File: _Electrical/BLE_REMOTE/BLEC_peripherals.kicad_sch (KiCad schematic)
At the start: 15 parts, among them J5 Conn_01x02_Pin, J9 Display, Q3 NPN, Q4 BSS806NEH6327XTSA1

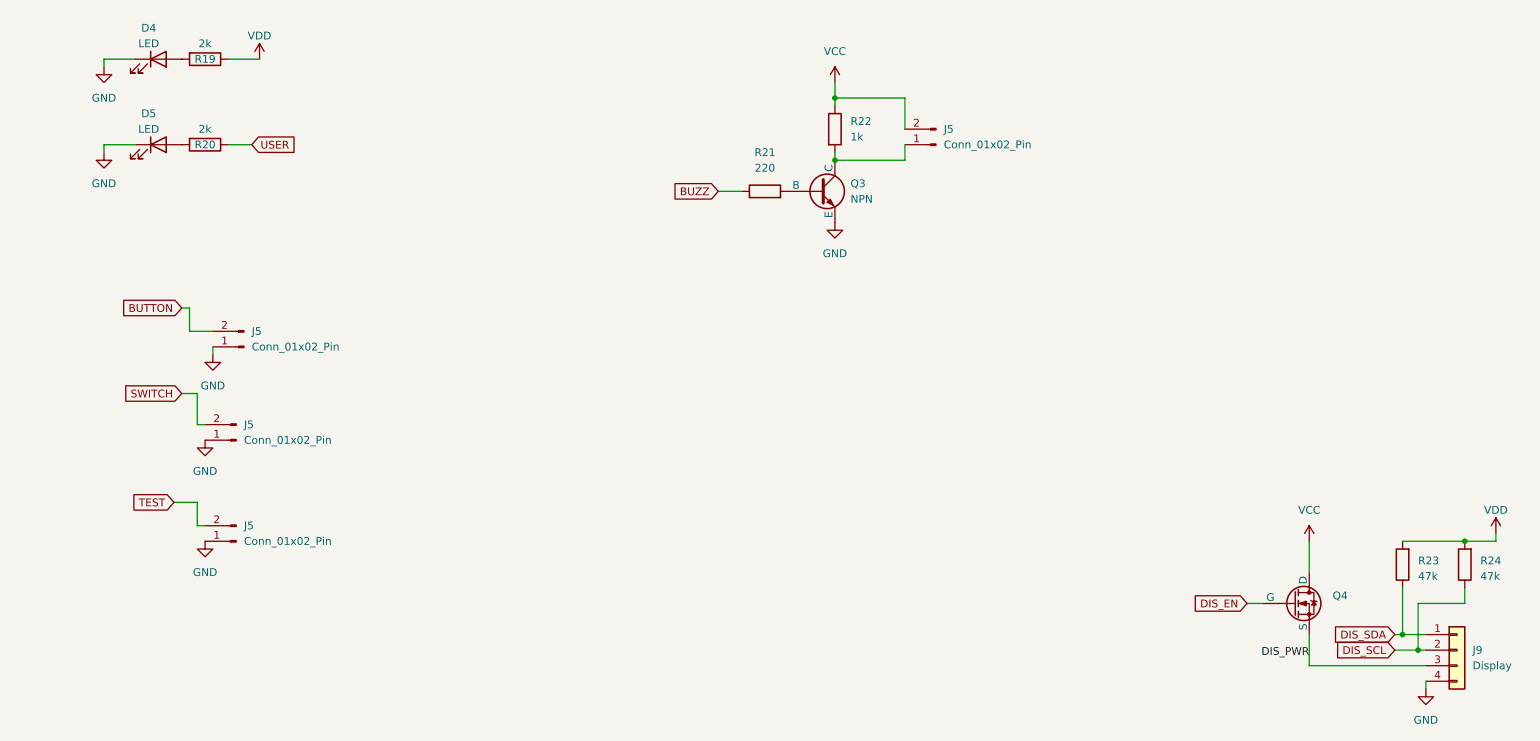
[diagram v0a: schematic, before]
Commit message: Added simulation and updated power button
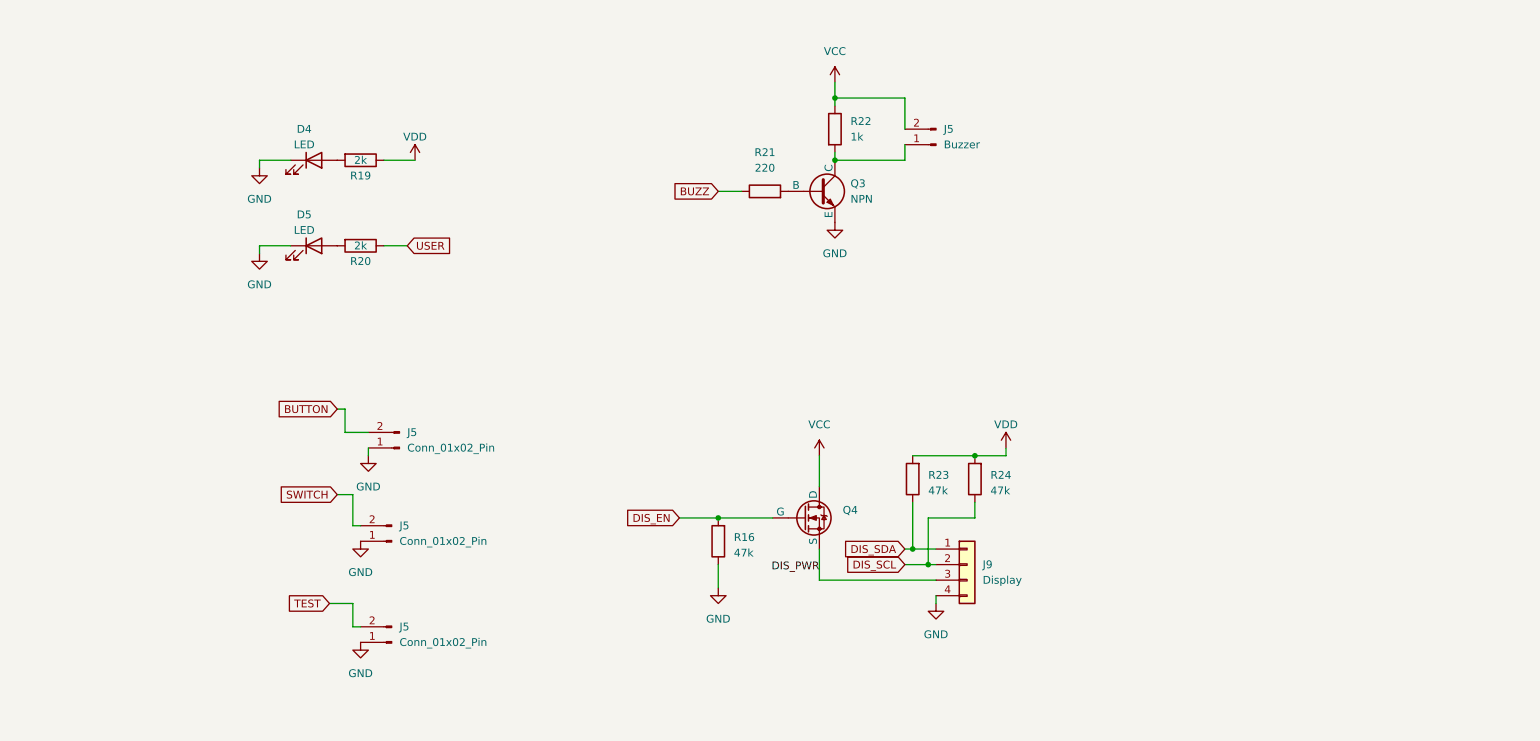
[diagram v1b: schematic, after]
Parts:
- added R16: 47k, Resistor_SMD:R_0402_1005Metric_Pad0.72x0.64mm_HandSolder, symbol Device:R
- J5: value Conn_01x02_Pin -> Buzzer
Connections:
- net DIS_EN: now also R16.2
- net GND: now also R16.1
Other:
- moved on the sheet: D4, D5, J5, J9, Q4, R19, R20, R23, R24

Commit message: started PCB design
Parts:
- renumbered D4 to D3, D5 to D4, J9 to J8, Q4 to Q1, Q3 to Q2, R19 to R13, R20 to R14, R16 to R15, R21 to R16, R22 to R17, R23 to R18, R24 to R19

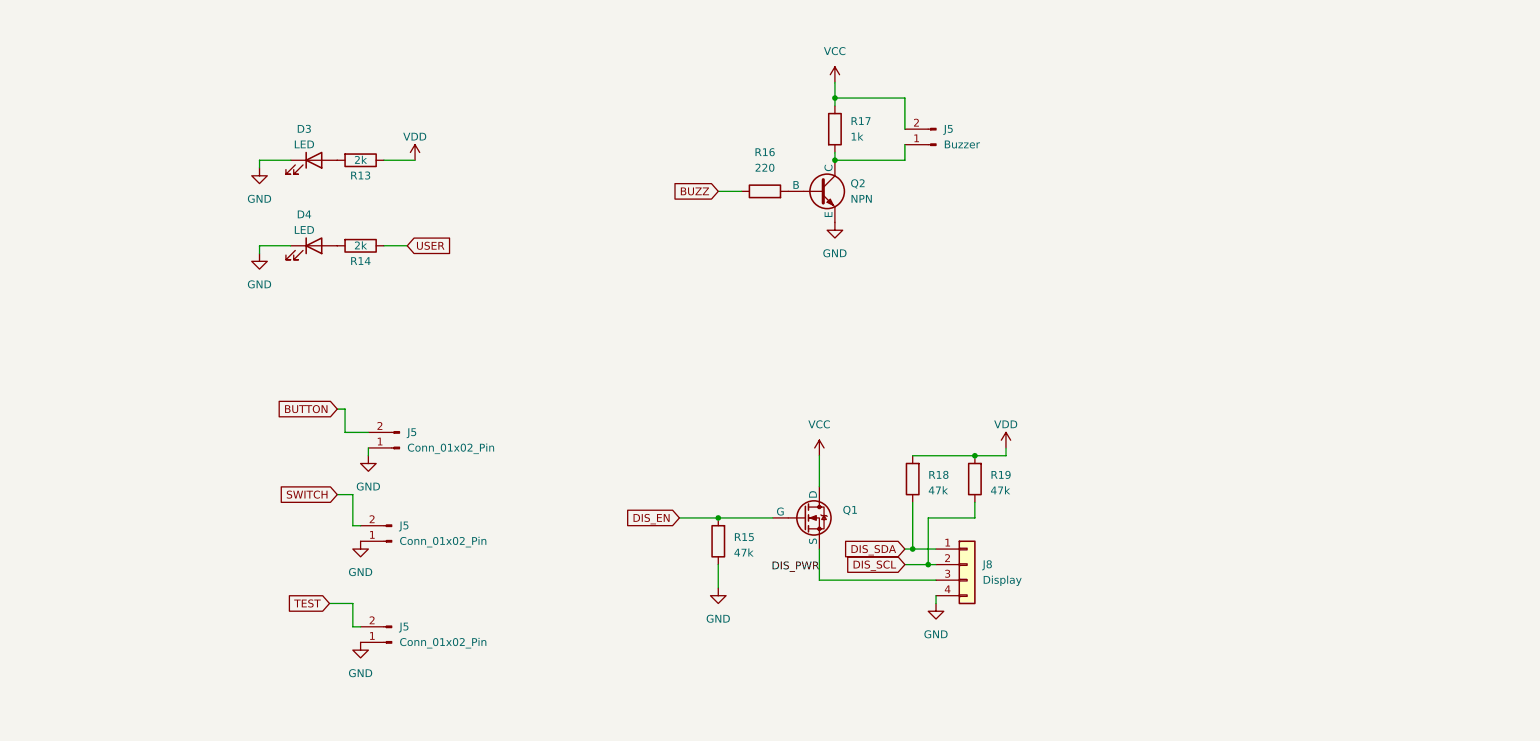
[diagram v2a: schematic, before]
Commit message: PCB parts placed
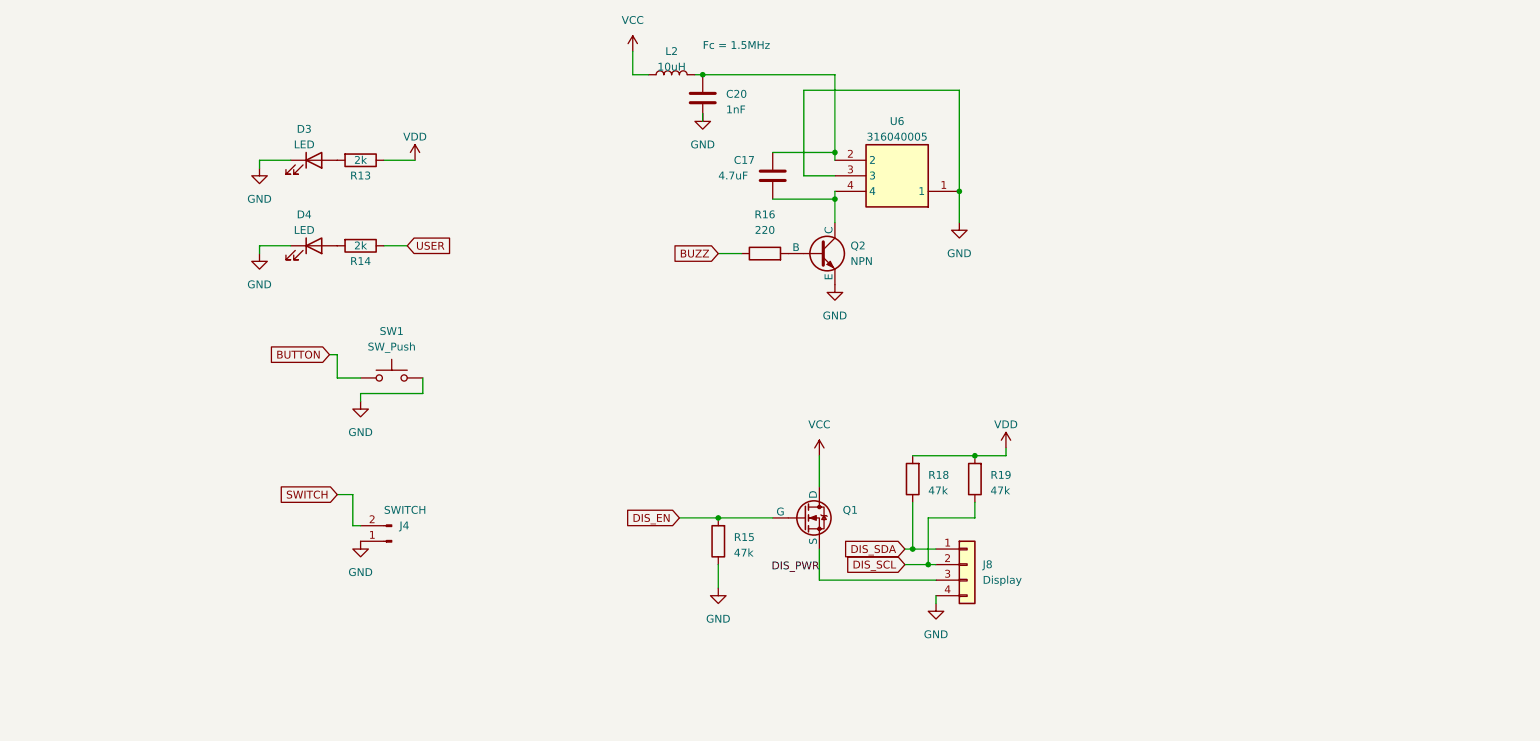
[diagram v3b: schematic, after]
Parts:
- removed J5: Buzzer, _Parts:2pad_conn_sm, symbol Connector:Conn_01x02_Pin
- removed J5 (x3): Conn_01x02_Pin, _Parts:2pad_conn_sm, symbol Connector:Conn_01x02_Pin
- removed R17: 1k, Resistor_SMD:R_0402_1005Metric_Pad0.72x0.64mm_HandSolder, symbol Device:R
- added C17: 4.7uF, Capacitor_SMD:C_0805_2012Metric_Pad1.18x1.45mm_HandSolder, symbol Device:C
- added C20: 1nF, Capacitor_SMD:C_0402_1005Metric_Pad0.74x0.62mm_HandSolder, symbol Device:C
- added J4: SWITCH, _Parts:2pad_conn_sm, symbol Connector:Conn_01x02_Pin
- added L2: 10uH, Inductor_SMD:L_0805_2012Metric_Pad1.15x1.40mm_HandSolder, symbol Device:L
- added SW1: SW_Push, Button_Switch_SMD:SW_Push_1P1T_NO_6x6mm_H9.5mm, symbol Switch:SW_Push
- added U6: 316040005, 316040005, symbol 316040005:316040005
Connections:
- net BUTTON: now also SW1.1
- net GND: now also C20.2, J4.1 (Pin_1), SW1.2, U6.1, U6.3
- net SWITCH: now also J4.2 (Pin_2)
- net VCC: now also L2.1
- net at Q2.1 (C): now also C17.2, U6.4
- new net: C17.1, C20.1, L2.2, U6.2
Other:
- note added: "Fc = 1.5MHz"
- moved on the sheet: Q2, R16

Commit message: JLCPCB parts selected
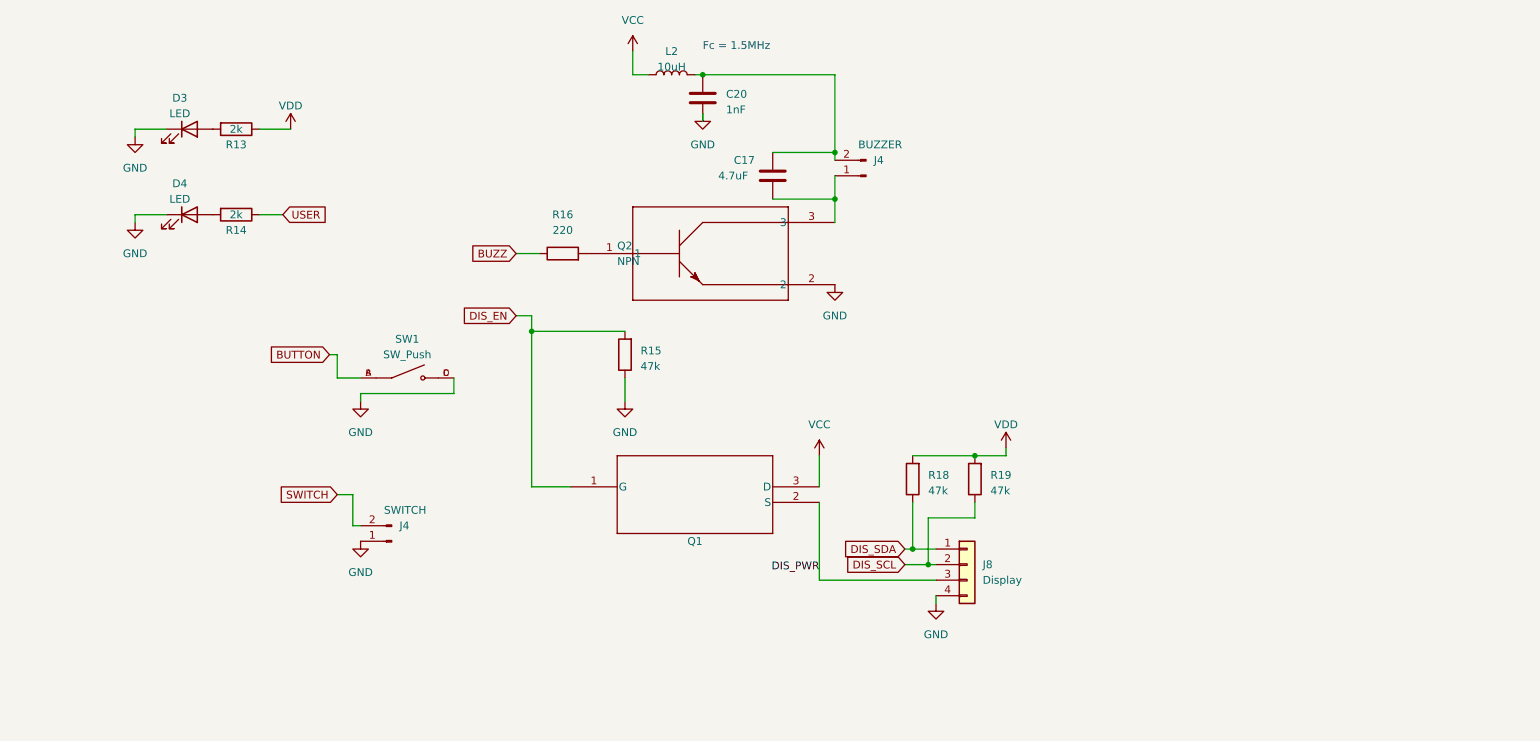
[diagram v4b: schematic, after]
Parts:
- removed U6: 316040005, 316040005, symbol 316040005:316040005
- added J4: BUZZER, _Parts:2pad_conn_sm, symbol Connector:Conn_01x02_Pin
- D3: JLCPCB Part# (none) -> C2290; LCSC Part # (none) -> C2290; Part LY L29K-H1K2-26-Z -> KT-0603W
- D4: JLCPCB Part# (none) -> C72038; LCSC Part # (none) -> C72038; Part LY L29K-H1K2-26-Z -> 19-213/Y2C-CQ2R2L/3T(CY)
- Q1: footprint _Parts:PG-SOT23-3-5_INF -> _Parts:SOT-23-3L_AOS; symbol Simulation_SPICE:NMOS -> AO3400A:AO3400A; JLCPCB Part# (none) -> C20917; LCSC Part # (none) -> C20917
- Q2: footprint Package_TO_SOT_SMD:TSOT-23 -> _Parts:TRAN_SS8050-G_CIP; symbol Simulation_SPICE:NPN -> SS8050:SS8050-G; JLCPCB Part# (none) -> C2150; LCSC Part # (none) -> C2150; Part MMBT3904-TP -> SS8050
- SW1: footprint Button_Switch_SMD:SW_Push_1P1T_NO_6x6mm_H9.5mm -> _Parts:SW_TS-1187A-B-A-B; symbol Switch:SW_Push -> TS-1187A-B-A-B:TS-1187A-B-A-B; Availability (none) -> Not in stock; Check_prices (none) -> https://www.snapeda.com/parts/TS-1187A-B-A-B/XKB+Industrial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; JLCPCB Part# (none) -> C318884; LCSC Part # (none) -> C102842; MANUFACTURER (none) -> XKB Industrial Precision; MAXIMUM_PACKAGE_HEIGHT (none) -> 1.5mm; MF (none) -> XKB Industrial Precision; MP (none) -> TS-1187A-B-A-B; PARTREV (none) -> A0; Package (none) -> Package; Part (none) -> TS-1187A-B-A-B; Price (none) -> None; STANDARD (none) -> Manufacturer Recommendations; SnapEDA_Link (none) -> https://www.snapeda.com/parts/TS-1187A-B-A-B/XKB+Industrial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
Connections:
- net BUTTON: now also SW1.A, SW1.B; no longer SW1.1
- net DIS_EN: now also Q1.1 (G); no longer Q1.2 (G)
- net DIS_PWR: now also Q1.2 (S); no longer Q1.3 (S)
- net GND: now also Q2.2, SW1.C, SW1.D; no longer Q2.3 (E), SW1.2
- net VCC: now also Q1.3 (D); no longer Q1.1 (D)
- net at C17.1, C20.1, L2.2: now also J4.2 (Pin_2)
- net at R16.2: now also Q2.1; no longer Q2.2 (B)
- net at C17.2: now also Q2.3, J4.1 (Pin_1); no longer Q2.1 (C)
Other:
- moved on the sheet: D3, D4, R13, R14, R15, R16

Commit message: Adjusted components and changed buttons
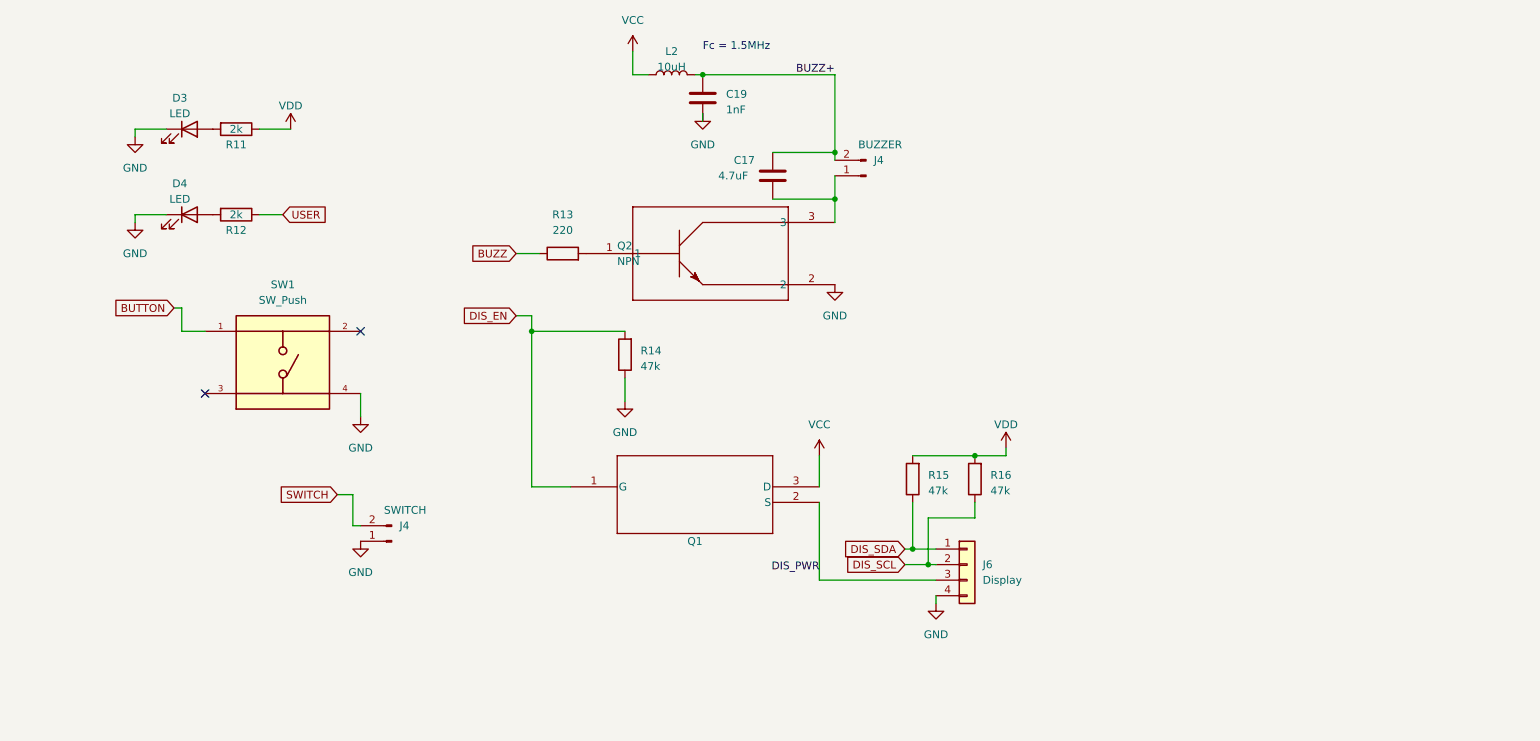
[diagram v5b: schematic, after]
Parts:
- removed SW1: SW_Push, _Parts:SW_TS-1187A-B-A-B, symbol TS-1187A-B-A-B:TS-1187A-B-A-B
- added SW1: SW_Push, _Parts:SW_TS02-66-120-BK-260-LCR-D, symbol TS02-66-120-BK-260-LCR-D:TS02-66-120-BK-260-LCR-D
- renumbered C20 to C19, J8 to J6, R13 to R11, R14 to R12, R16 to R13, R15 to R14, R18 to R15, R19 to R16
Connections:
- net BUTTON: now also SW1.1
- net GND: now also SW1.4
- net BUZZ+: now reaches C17.1, C19.1, J4.2 (Pin_2), L2.2
- no-connect marks 0 -> 2
